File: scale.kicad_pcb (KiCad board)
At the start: 4 copper layers, 80 x 60 mm, 53 parts, among them J1 Conn_01x02_Pin, J2 Conn_01x04_Pin, J3 Conn_01x05_Pin, J4 Conn_01x05_Pin, Q1 S8050, Q2 S8050, Q3 MMBT3904, SW1 SW_Push, U1 HLK-10M12, U2 LM2576HVS-5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

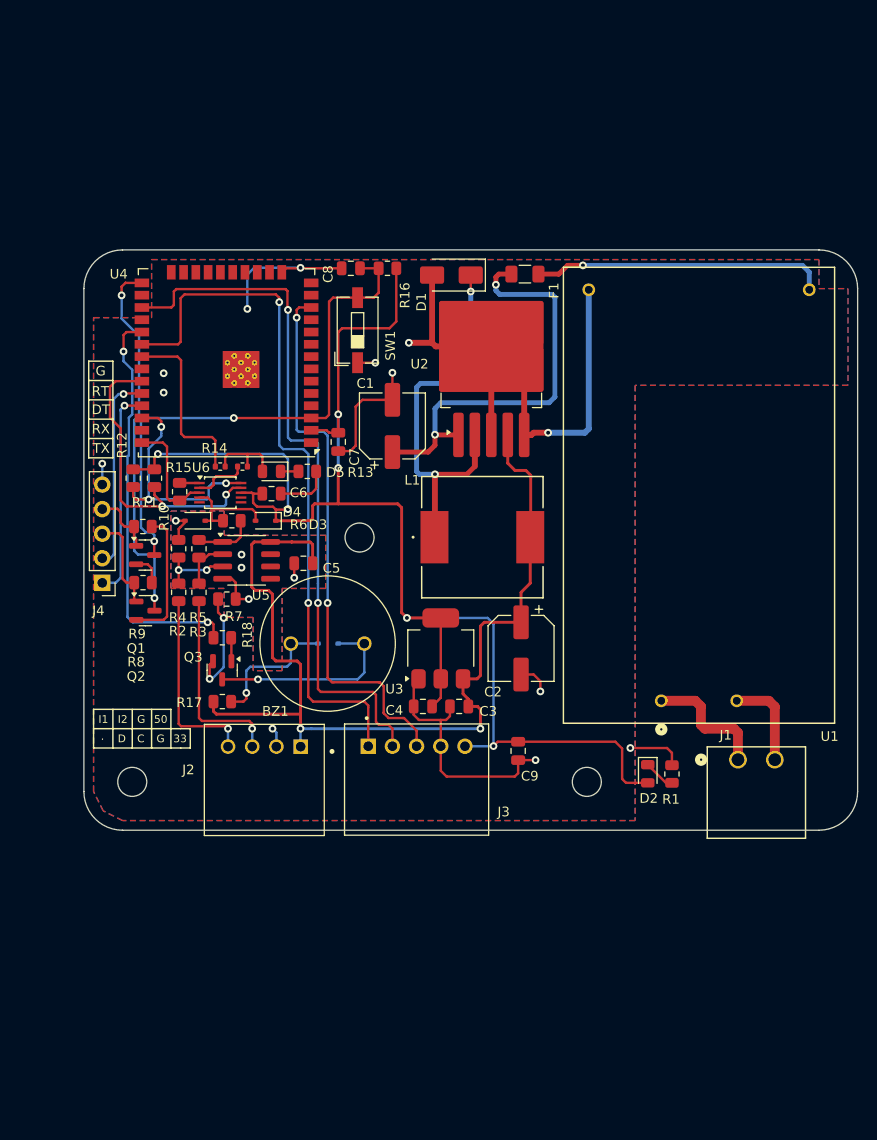
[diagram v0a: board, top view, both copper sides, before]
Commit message: change dimensions
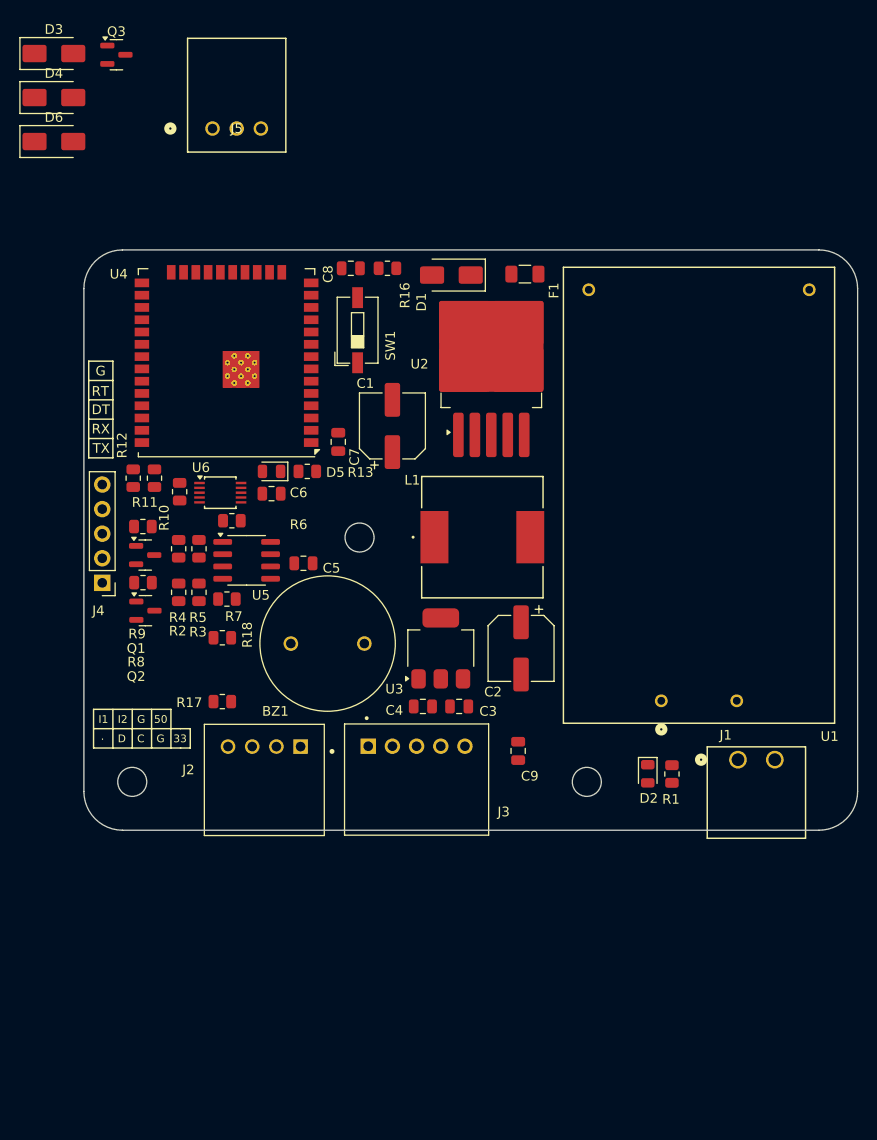
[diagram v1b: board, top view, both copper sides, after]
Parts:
- removed R14, R15: 0, Resistor_SMD:R_0402_1005Metric
- added J5: Conn_01x03_Pin, BBG:CONN_S3B-XH-ALFSN_JST, F.Cu at (13.3, -12.6)
- D3, D4: value BAT60A -> D_Zener; footprint Diode_SMD:D_SOD-323 -> Diode_SMD:D_SMA
- D6: value BAT60A -> D_Zener; footprint Diode_SMD:D_SOD-323 -> Diode_SMD:D_SMA; moved to F.Cu
- Q3: value MMBT3904 -> S8050
- moved Q3 64.6 mm to (3.36, -20.2), turned to 0 degrees
- moved D6 59.1 mm to (-3.10, -11.2)
- moved D3 53.0 mm to (-3.10, -20.3), turned to 0 degrees
- moved D4 46.1 mm to (-3.10, -15.8), turned to 0 degrees
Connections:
- D5 pad 2: Net-(D5-A) -> /weighing_unit/RDY
- Q3 pad 1: Net-(Q3-B) -> GND
- Q3 pad 2: GND -> Net-(Q3-B)
- R13 pad 1: Net-(D5-K) -> GND
- R13 pad 2: GND -> Net-(D5-K)
- U4 pad 13: unconnected-(U4-IO14-Pad13) -> /BT1
- U4 pad 16: unconnected-(U4-IO13-Pad16) -> /BT0
- U4 pad 31: /RDY_MCU -> unconnected-(U4-IO19-Pad31)
- U6 pad 2: /RDY_ADC -> /weighing_unit/RDY
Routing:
- net GND: track 162.3 -> 0.00 mm, vias 14 -> 0
- net +3V3: track 150.1 -> 0.00 mm, vias 6 -> 0
- net +5V: track 101.2 -> 0.00 mm, vias 2 -> 0
- net /display/DATA: track 73.5 -> 0.00 mm, vias 2 -> 0
- net /display/DOT: track 73.5 -> 0.00 mm, vias 2 -> 0
- net /display/CLOCK: track 57.1 -> 0.00 mm, vias 2 -> 0
- net /mcu/EN: track 56.2 -> 0.00 mm, vias 2 -> 0
- net Net-(U2-VIN): track 43.6 -> 0.00 mm, vias 2 -> 0
- net /BUZZ: track 42.3 -> 0.00 mm, vias 2 -> 0
- net Net-(D1-K): track 41.1 -> 0.00 mm, vias 2 -> 0
- net /mcu/IO0: track 38.4 -> 0.00 mm, vias 2 -> 0
- net /mcu/SDA: track 32.2 -> 0.00 mm, vias 2 -> 0
- net Net-(U1-+VO): track 30.5 -> 0.00 mm, vias 1 -> 0
- net /mcu/SCL: track 24.5 -> 0.00 mm, vias 3 -> 0
- net /TXD: track 21.9 -> 0.00 mm, vias 1 -> 0
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- removed copper zone on B.Cu, net GND
- removed copper zone on F.Cu, net GND
- removed copper zone on In1.Cu, net GND
- removed copper zone on In2.Cu, net GND
- removed copper zone on B.Cu, net GNDA
- removed copper zone on F.Cu, net GNDA

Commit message: done component placement
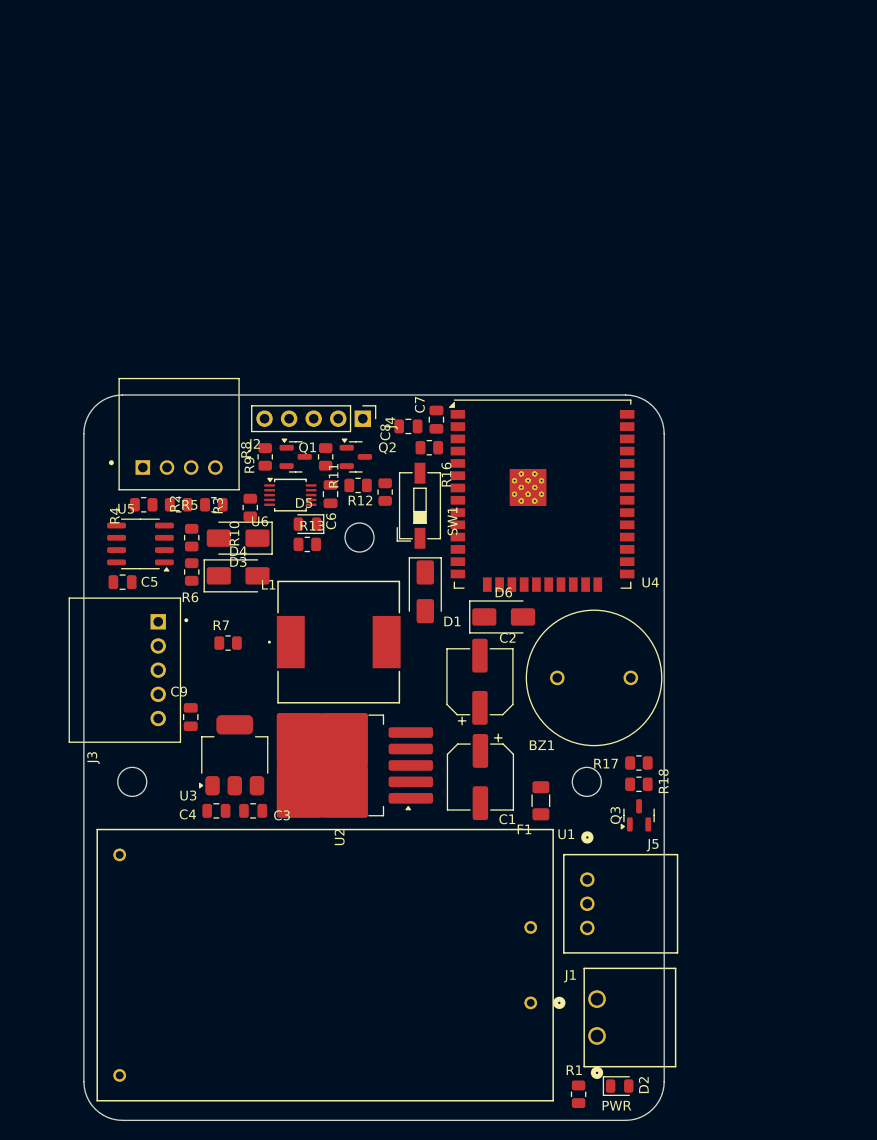
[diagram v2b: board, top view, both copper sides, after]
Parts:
- moved Q3 95.4 mm to (57.4, 58.5), turned to 90 degrees
- moved J5 86.8 mm to (52.1, 65.1), turned to -90 degrees
- moved D6 67.7 mm to (43.4, 38.0)
- moved F1 54.5 mm to (47.2, 57.0), turned to 90 degrees
- moved D3 53.6 mm to (15.9, 29.8), turned to 180 degrees
- moved D4 53.0 mm to (15.9, 33.7)
- moved R18 45.7 mm to (57.4, 55.2)
- moved U2 44.8 mm to (26.1, 53.3), turned to 180 degrees
- moved R17 43.5 mm to (57.4, 53.0)
- moved C1 37.4 mm to (41.0, 54.5), turned to -90 degrees
- moved U4 35.4 mm to (47.4, 25.2), turned to 0 degrees
- moved R1 34.5 mm to (51.1, 87.3), turned to -90 degrees
- moved C9 34.0 mm to (11.1, 48.3), turned to 90 degrees
- moved U1 34.0 mm to (46.2, 77.8), turned to 180 degrees
- moved D1 32.9 mm to (35.3, 35.4), turned to -90 degrees
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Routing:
- removed copper zone on In1.Cu, net GNDA
- removed copper zone on In2.Cu, net GNDA
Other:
- board size 80 x 60 mm -> 60 x 75 mm
- board text added: "PWR"
- board text removed: "."
- board text removed: "33"
- board text removed: "50"
- board text removed: "C"
- board text removed: "D"
- board text removed: "DT"
- board text removed: "G"
- board text removed: "I1"
- board text removed: "I2"
- board text removed: "RT"
- board text removed: "RX"
- board text removed: "TX"

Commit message: finish routing
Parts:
- moved U1 1.08 mm to (46.5, 78.9)
- moved J5 1.04 mm to (53.1, 65.4)
- moved R18 0.95 mm to (57.4, 54.3)
- moved R17 0.80 mm to (57.4, 52.2)
- moved J3 0.69 mm to (7.00, 43.5)
- moved R11 0.65 mm to (28.3, 25.0)
- moved R10 0.65 mm to (17.3, 26.0)
- moved C9 0.60 mm to (10.8, 47.8)
- moved D5 0.50 mm to (23.1, 28.9)
- moved J4 0.45 mm to (28.5, 17.1)
- moved R13 0.45 mm to (23.1, 30.9)
- moved J2 0.45 mm to (9.65, 22.1)
- moved Q2 0.28 mm to (27.8, 21.4)
- moved R8 0.20 mm to (24.8, 21.4)
- moved Q1 0.14 mm to (21.8, 21.4)
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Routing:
- net +3V3: track 0.00 -> 159.3 mm, vias 0 -> 7
- net +5V: track 0.00 -> 113.8 mm, vias 0 -> 3
- net GND: track 0.00 -> 75.4 mm, vias 0 -> 19
- net /display/DOT: track 0.00 -> 59.7 mm, vias 0 -> 1
- net /display/DATA: track 0.00 -> 58.3 mm, vias 0 -> 1
- net /BT1: track 0.00 -> 49.2 mm, vias 0 -> 1
- net Net-(U1-+VO): track 0.00 -> 48.0 mm, vias 0 -> 1
- net /mcu/SDA: track 0.00 -> 47.3 mm, vias 0 -> 2
- net /display/CLOCK: track 0.00 -> 43.3 mm, vias 0 -> 1
- net /BT0: track 0.00 -> 43.1 mm, vias 0 -> 1
- net /mcu/SCL: track 0.00 -> 42.0 mm, vias 0 -> 3
- net Net-(D1-K): track 0.00 -> 37.8 mm, vias 0 -> 2
- net /mcu/IO0: track 0.00 -> 37.0 mm, vias 0 -> 2
- net GNDA: track 0.00 -> 36.7 mm, vias 0 -> 3
- net /RXD: track 0.00 -> 34.9 mm, vias 0 -> 1
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- added copper zone on B.Cu, net GND
- added copper zone on F.Cu, net GND
- added copper zone on In1.Cu, net GND
- added copper zone on In2.Cu, net GND
- added copper zone on B.Cu, net GNDA
- added copper zone on F.Cu, net GNDA
- added copper zone on In1.Cu, net GNDA
- added copper zone on In2.Cu, net GNDA

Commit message: add some silkscreen, enable access to BOOT pin
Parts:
- added R14: 0, Resistor_SMD:R_0805_2012Metric, F.Cu at (58.5, 36.7)
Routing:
- net /mcu/IO0: track 37.0 -> 41.3 mm
- net GND: track 75.4 -> 78.9 mm, vias 19 -> 20
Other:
- board text added: "+5v"
- board text added: "."
- board text added: "3v3"
- board text added: "archerfish"
- board text added: "bt0"
- board text added: "bt1"
- board text added: "clk"
- board text added: "dat"
- board text added: "elektronik"
- board text added: "gnd"
- board text added: "gnda"
- board text added: "in1"
- board text added: "in2"
- board text added: "scale.2024.10.0.1.1"
